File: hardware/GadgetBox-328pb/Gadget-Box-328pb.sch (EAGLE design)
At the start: 34 parts, among them IC1A ATMEGA328PB-AU, IC1B ATMEGA328PB-MU, U1 MCP73831T-2ACI/OT, U2 AP2112-3.3, X1 CRYSTAL-0500290P1

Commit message: Connect VCC from USB connector to 5V0. Ooops!
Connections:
- removed net VBUS: USB1.VCC
- net 5V0: now also USB1.VCC
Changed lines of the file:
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@@
 <wire x1="12.7" y1="144.78" x2="15.24" y2="144.78" width="0.2032" layer="91"/>
+</segment>
+<segment>
+<pinref part="USB1" gate="USB" pin="VCC"/>
+<pinref part="U$1" gate="G$1" pin="VBUS"/>
+<wire x1="113.03" y1="60.96" x2="113.03" y2="55.88" width="0.1524" layer="91"/>
 </segment>
 </net>
@@
 </segment>
 </net>
-<net name="VBUS" class="0">
-<segment>
-<pinref part="USB1" gate="USB" pin="VCC"/>
-<pinref part="U$1" gate="G$1" pin="VBUS"/>
-<wire x1="113.03" y1="60.96" x2="113.03" y2="55.88" width="0.1524" layer="91"/>
-</segment>
-</net>

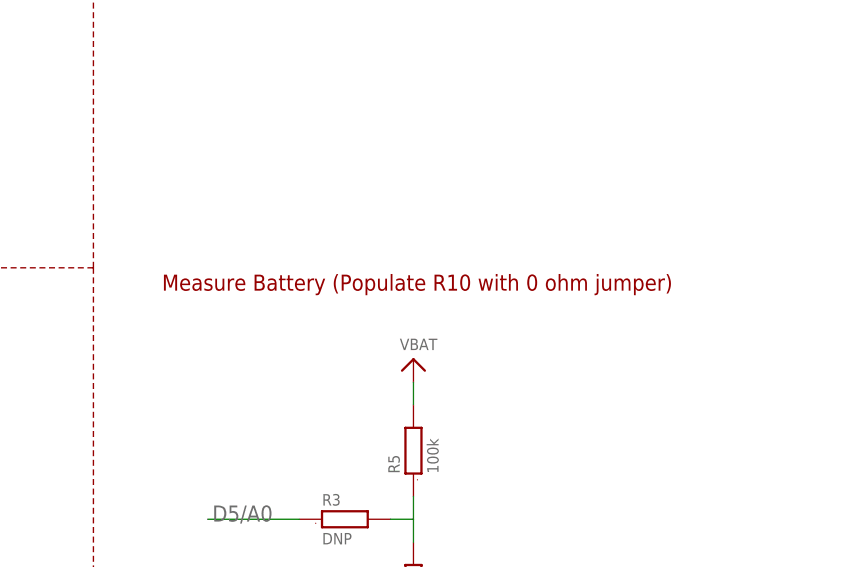
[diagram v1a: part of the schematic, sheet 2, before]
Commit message: minor typo in schematic note
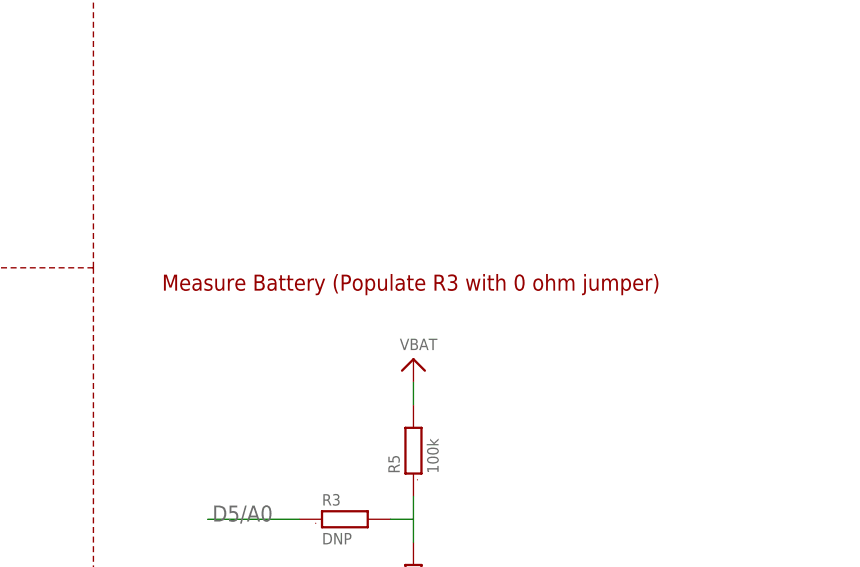
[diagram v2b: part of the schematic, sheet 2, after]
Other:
- note added: "Measure Battery (Populate R3 with 0 ohm jumper)"
- note removed: "Measure Battery (Populate R10 with 0 ohm jumper)"
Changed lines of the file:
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@@
 <text x="48.26" y="116.84" size="1.778" layer="94">BATTERY CHARGE &amp; MONITOR</text>
 <wire x1="5.08" y1="71.12" x2="134.62" y2="71.12" width="0.1524" layer="94" style="shortdash"/>
-<text x="142.24" y="119.38" size="1.778" layer="94">Measure Battery (Populate R10 with 0 ohm jumper)</text>
+<text x="142.24" y="119.38" size="1.778" layer="94">Measure Battery (Populate R3 with 0 ohm jumper)</text>
 <text x="5.08" y="10.16" size="1.778" layer="91">Attribution: The charging and power sections are from Adafruit Feather Huzzah design.</text>
 </plain>

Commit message: wip
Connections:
- net 5V0: no longer AH.5V@0, AL.5V@0, BH.5V@0, BL.5V@0
- net RESET: no longer AH.RESET@1, AL.RESET@1, BH.RESET@1, BL.RESET@1
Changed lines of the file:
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@@
 <grid distance="0.1" unitdist="inch" unit="inch" style="lines" multiple="1" display="no" altdistance="0.01" altunitdist="inch" altunit="inch"/>
 <layers>
-<layer number="1" name="Top" color="4" fill="1" visible="no" active="no"/>
-<layer number="2" name="Route2" color="1" fill="3" visible="no" active="no"/>
-<layer number="3" name="Route3" color="4" fill="3" visible="no" active="no"/>
-<layer number="14" name="Route14" color="1" fill="6" visible="no" active="no"/>
-<layer number="15" name="Route15" color="4" fill="6" visible="no" active="no"/>
-<layer number="16" name="Bottom" color="1" fill="1" visible="no" active="no"/>
-<layer number="17" name="Pads" color="2" fill="1" visible="no" active="no"/>
-<layer number="18" name="Vias" color="2" fill="1" visible="no" active="no"/>
-<layer number="19" name="Unrouted" color="6" fill="1" visible="no" active="no"/>
-<layer number="20" name="Dimension" color="15" fill="1" visible="no" active="no"/>
-<layer number="21" name="tPlace" color="16" fill="1" visible="no" active="no"/>
-<layer number="22" name="bPlace" color="14" fill="1" visible="no" active="no"/>
-<layer number="23" name="tOrigins" color="15" fill="1" visible="no" active="no"/>
-<layer number="24" name="bOrigins" color="15" fill="1" visible="no" active="no"/>
-<layer number="25" name="tNames" color="16" fill="1" visible="no" active="no"/>
-<layer number="26" name="bNames" color="7" fill="1" visible="no" active="no"/>
-<layer number="27" name="tValues" color="7" fill="1" visible="no" active="no"/>
-<layer number="28" name="bValues" color="7" fill="1" visible="no" active="no"/>
+<layer number="1" name="Top" color="4" fill="1" visible="yes" active="no"/>
+<layer number="2" name="Route2" color="1" fill="3" visible="yes" active="no"/>
+<layer number="3" name="Route3" color="4" fill="3" visible="yes" active="no"/>
+<layer number="14" name="Route14" color="1" fill="6" visible="yes" active="no"/>
+<layer number="15" name="Route15" color="4" fill="6" visible="yes" active="no"/>
+<layer number="16" name="Bottom" color="1" fill="1" visible="yes" active="no"/>
+<layer number="17" name="Pads" color="2" fill="1" visible="yes" active="no"/>
+<layer number="18" name="Vias" color="2" fill="1" visible="yes" active="no"/>
+<layer number="19" name="Unrouted" color="6" fill="1" visible="yes" active="no"/>
+<layer number="20" name="Dimension" color="15" fill="1" visible="yes" active="no"/>
+<layer number="21" name="tPlace" color="16" fill="1" visible="yes" active="no"/>
+<layer number="22" name="bPlace" color="14" fill="1" visible="yes" active="no"/>
+<layer number="23" name="tOrigins" color="15" fill="1" visible="yes" active="no"/>
+<layer number="24" name="bOrigins" color="15" fill="1" visible="yes" active="no"/>
+<layer number="25" name="tNames" color="16" fill="1" visible="yes" active="no"/>
+<layer number="26" name="bNames" color="7" fill="1" visible="yes" active="no"/>
+<layer number="27" name="tValues" color="7" fill="1" visible="yes" active="no"/>
+<layer number="28" name="bValues" color="7" fill="1" visible="yes" active="no"/>
 <layer number="29" name="tStop" color="7" fill="3" visible="no" active="no"/>
 <layer number="30" name="bStop" color="7" fill="6" visible="no" active="no"/>
@@
 <layer number="35" name="tGlue" color="7" fill="4" visible="no" active="no"/>
 <layer number="36" name="bGlue" color="7" fill="5" visible="no" active="no"/>
-<layer number="37" name="tTest" color="7" fill="1" visible="no" active="no"/>
-<layer number="38" name="bTest" color="7" fill="1" visible="no" active="no"/>
+<layer number="37" name="tTest" color="7" fill="1" visible="yes" active="no"/>
+<layer number="38" name="bTest" color="7" fill="1" visible="yes" active="no"/>
 <layer number="39" name="tKeepout" color="4" fill="11" visible="no" active="no"/>
 <layer number="40" name="bKeepout" color="1" fill="11" visible="no" active="no"/>
@@
 <layer number="44" name="Drills" color="7" fill="1" visible="no" active="no"/>
 <layer number="45" name="Holes" color="7" fill="1" visible="no" active="no"/>
-<layer number="46" name="Milling" color="3" fill="1" visible="no" active="no"/>
-<layer number="47" name="Measures" color="7" fill="1" visible="no" active="no"/>
-<layer number="48" name="Document" color="7" fill="1" visible="no" active="no"/>
-<layer number="49" name="Reference" color="7" fill="1" visible="no" active="no"/>
-<layer number="50" name="dxf" color="7" fill="1" visible="no" active="no"/>
-<layer number="51" name="tDocu" color="6" fill="1" visible="no" active="no"/>
-<layer number="52" name="bDocu" color="7" fill="1" visible="no" active="no"/>
-<layer number="53" name="tGND_GNDA" color="7" fill="1" visible="no" active="no"/>
-<layer number="54" name="bGND_GNDA" color="7" fill="1" visible="no" active="no"/>
-<layer number="56" name="wert" color="7" fill="1" visible="no" active="no"/>
-<layer number="57" name="tCAD" color="7" fill="1" visible="no" active="no"/>
-<layer number="59" name="tCarbon" color="7" fill="1" visible="no" active="no"/>
-<layer number="60" name="bCarbon" color="7" fill="1" visible="no" active="no"/>
+<layer number="46" name="Milling" color="3" fill="1" visible="yes" active="no"/>
+<layer number="47" name="Measures" color="7" fill="1" visible="yes" active="no"/>
+<layer number="48" name="Document" color="7" fill="1" visible="yes" active="no"/>
+<layer number="49" name="Reference" color="7" fill="1" visible="yes" active="no"/>
+<layer number="50" name="dxf" color="7" fill="1" visible="yes" active="no"/>
+<layer number="51" name="tDocu" color="6" fill="1" visible="yes" active="no"/>
+<layer number="52" name="bDocu" color="7" fill="1" visible="yes" active="no"/>
+<layer number="53" name="tGND_GNDA" color="7" fill="1" visible="yes" active="no"/>
+<layer number="54" name="bGND_GNDA" color="7" fill="1" visible="yes" active="no"/>
+<layer number="56" name="wert" color="7" fill="1" visible="yes" active="no"/>
+<layer number="57" name="tCAD" color="7" fill="1" visible="yes" active="no"/>
+<layer number="59" name="tCarbon" color="7" fill="1" visible="yes" active="no"/>
+<layer number="60" name="bCarbon" color="7" fill="1" visible="yes" active="no"/>
 <layer number="90" name="Modules" color="7" fill="1" visible="yes" active="yes"/>
 <layer number="91" name="Nets" color="2" fill="1" visible="yes" active="yes"/>
@@
 </part>
 <part name="5V0_PWR2" library="GadgetFactory" deviceset="5V0" device=""/>
-<part name="5V0_PWR3" library="GadgetFactory" deviceset="5V0" device=""/>
-<part name="5V0_PWR4" library="GadgetFactory" deviceset="5V0" device=""/>
-<part name="5V0_PWR5" library="GadgetFactory" deviceset="5V0" device=""/>
 <part name="R4" library="GadgetFactory" deviceset="R" device="0603" value="10K">
 <attribute name="PARTNO" value="RC0603JR-0710KL,YAGEO (VA),dk,311-10KGRCT-ND,RES SMD 10K OHM 5% 1/10W 0603 , REF36"/>
@@
 <instance part="GND9" gate="A" x="157.48" y="66.04" rot="R180"/>
 <instance part="3V3_PWR9" gate="A" x="111.76" y="109.22"/>
-<instance part="5V0_PWR2" gate="A" x="104.648" y="113.284"/>
-<instance part="5V0_PWR3" gate="A" x="151.892" y="72.136" rot="R180"/>
-<instance part="5V0_PWR4" gate="A" x="151.892" y="28.956" rot="R180"/>
-<instance part="5V0_PWR5" gate="A" x="104.648" y="70.104"/>
+<instance part="5V0_PWR2" gate="A" x="104.648" y="123.444"/>
 <instance part="R4" gate="A" x="193.04" y="96.52" rot="R90">
 <attribute name="PARTNO" x="193.04" y="96.52" size="1.778" layer="96" display="off"/>
@@
 <net name="RESET" class="0">
 <segment>
-<wire x1="106.68" y1="119.38" x2="107.188" y2="119.38" width="0.2032" layer="91"/>
 <label x="111.76" y="119.507" size="1.27" layer="95" xref="yes"/>
-<pinref part="BH" gate="ECOG$1" pin="RESET@1"/>
-<wire x1="107.188" y1="119.38" x2="111.76" y2="119.38" width="0.2032" layer="91"/>
-<wire x1="107.188" y1="110.744" x2="107.188" y2="119.38" width="0.2032" layer="91"/>
-</segment>
-<segment>
-<pinref part="AL" gate="ECOG$1" pin="RESET@1"/>
-<wire x1="149.352" y1="74.676" x2="149.352" y2="70.612" width="0.2032" layer="91"/>
-<wire x1="149.352" y1="70.612" x2="141.732" y2="70.612" width="0.2032" layer="91"/>
-<label x="142.113" y="70.358" size="1.27" layer="95" rot="R180" xref="yes"/>
-</segment>
-<segment>
-<label x="111.76" y="72.644" size="1.27" layer="95" xref="yes"/>
-<pinref part="BL" gate="ECOG$1" pin="RESET@1"/>
-<wire x1="107.188" y1="72.644" x2="111.76" y2="72.644" width="0.2032" layer="91"/>
-<wire x1="107.188" y1="67.564" x2="107.188" y2="72.644" width="0.2032" layer="91"/>
-</segment>
-<segment>
-<pinref part="AH" gate="ECOG$1" pin="RESET@1"/>
-<wire x1="149.352" y1="31.496" x2="149.352" y2="26.924" width="0.2032" layer="91"/>
-<wire x1="149.352" y1="26.924" x2="141.478" y2="26.924" width="0.2032" layer="91"/>
-<wire x1="141.478" y1="26.924" x2="141.478" y2="27.178" width="0.2032" layer="91"/>
-<label x="141.859" y="26.797" size="1.27" layer="95" rot="R180" xref="yes"/>
+<wire x1="106.68" y1="119.38" x2="111.76" y2="119.38" width="0.2032" layer="91"/>
 </segment>
 </net>
@@
 </segment>
 </net>
-<net name="5V0" class="0">
-<segment>
-<pinref part="BH" gate="ECOG$1" pin="5V@0"/>
-<pinref part="5V0_PWR2" gate="A" pin="5V0"/>
-</segment>
-<segment>
-<pinref part="AL" gate="ECOG$1" pin="5V@0"/>
-<pinref part="5V0_PWR3" gate="A" pin="5V0"/>
-</segment>
-<segment>
-<pinref part="AH" gate="ECOG$1" pin="5V@0"/>
-<pinref part="5V0_PWR4" gate="A" pin="5V0"/>
-</segment>
-<segment>
-<pinref part="BL" gate="ECOG$1" pin="5V@0"/>
-<pinref part="5V0_PWR5" gate="A" pin="5V0"/>
-</segment>
-</net>
